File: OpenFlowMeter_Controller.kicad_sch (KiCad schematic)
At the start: 8 parts, among them J3 Conn_01x06, J5 Conn_01x03, U2 STM32F103C8Tx

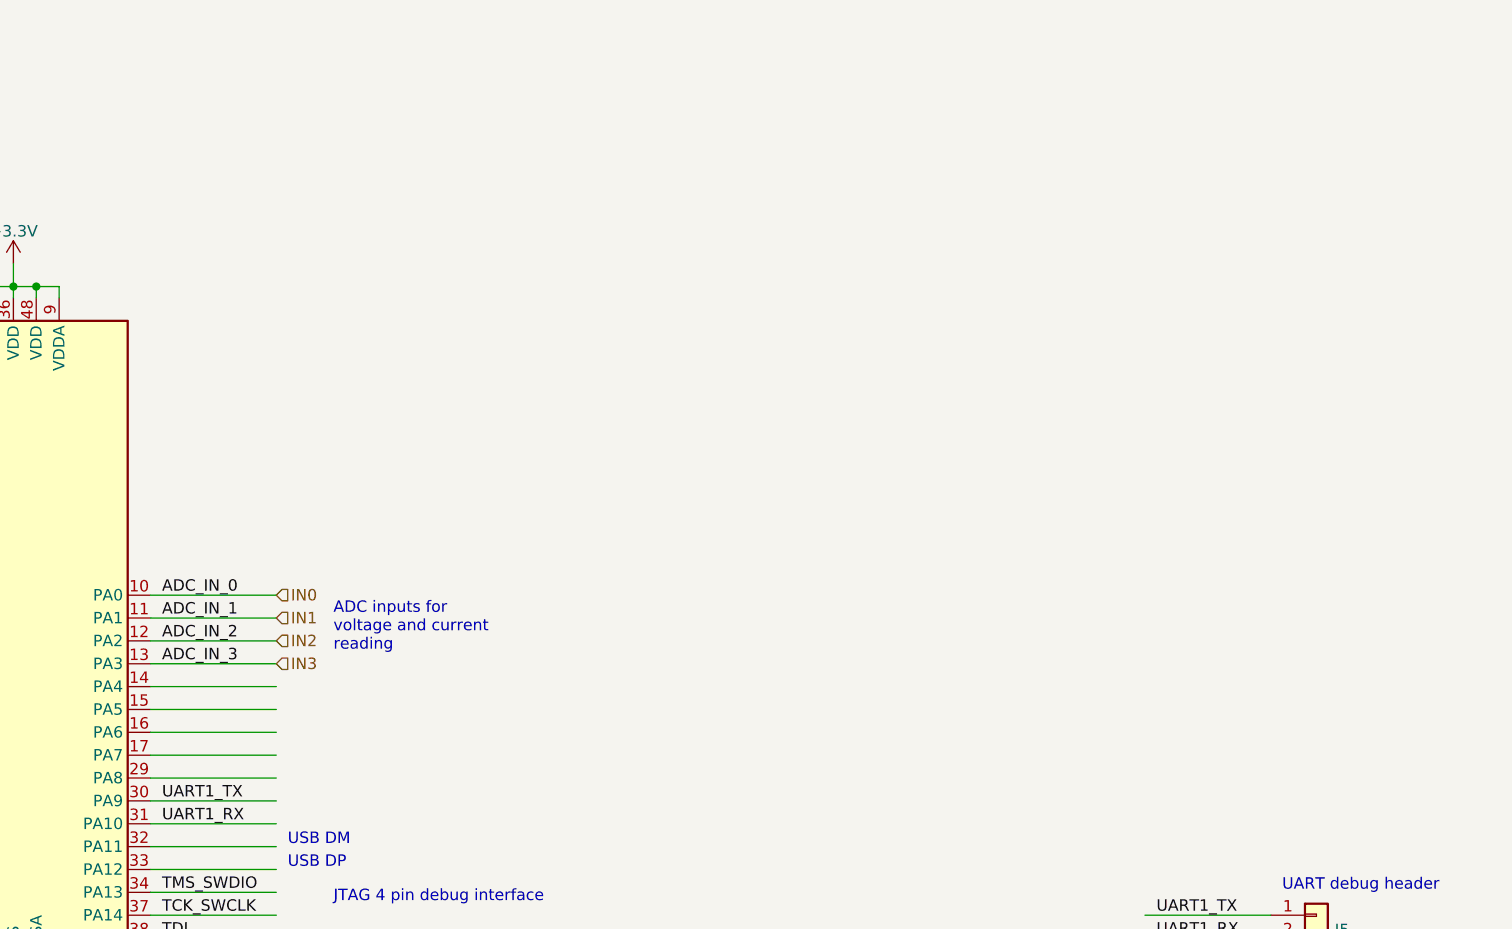
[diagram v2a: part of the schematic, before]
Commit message: added CAN Transceiver
added SN65HVD231 3.3V CAN Transceiver in order to connect multiple flow meter to a single bus.
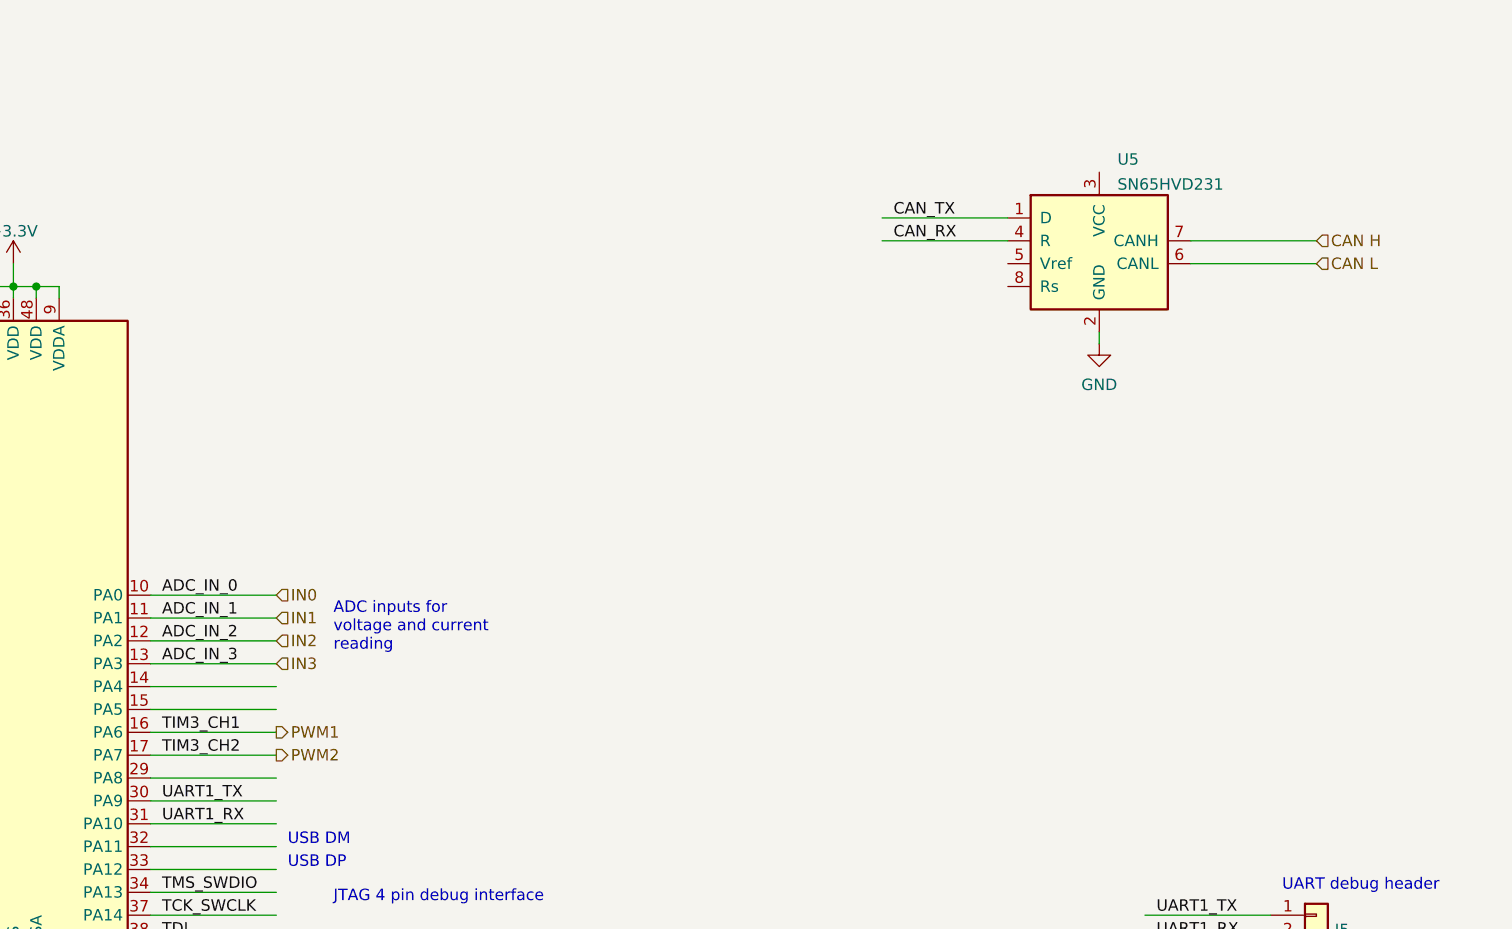
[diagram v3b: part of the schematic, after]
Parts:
- added U5: SN65HVD231, Package_SO:SOIC-8_3.9x4.9mm_P1.27mm, symbol Interface_CAN_LIN:SN65HVD231
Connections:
- net CAN_RX: now also U5.4 (R)
- net CAN_TX: now also U5.1 (D)
- net GND: now also U5.2 (GND)
- net PWM1: now reaches U2.16 (PA6)
- net PWM2: now reaches U2.17 (PA7)
- new net CAN H: U5.7 (CANH)
- new net CAN L: U5.6 (CANL)
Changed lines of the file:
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@@
+    (stroke (width 0) (type default) (color 0 0 0 0))
+  )
+  (wire (pts (xy 251.46 46.99) (xy 265.43 46.99))
     (stroke (width 0) (type default) (color 0 0 0 0))
   )
@@
     (stroke (width 0) (type default) (color 0 0 0 0))
   )
+  (wire (pts (xy 217.17 41.91) (xy 231.14 41.91))
+    (stroke (width 0) (type default) (color 0 0 0 0))
+  )
   (wire (pts (xy 260.35 124.46) (xy 259.08 124.46))
     (stroke (width 0) (type default) (color 0 0 0 0))
@@
     (stroke (width 0) (type default) (color 0 0 0 0))
   )
+  (wire (pts (xy 217.17 44.45) (xy 231.14 44.45))
+    (stroke (width 0) (type default) (color 0 0 0 0))
+  )
   (wire (pts (xy 88.9 111.76) (xy 102.87 111.76))
     (stroke (width 0) (type default) (color 0 0 0 0))
   )
+  (wire (pts (xy 241.3 54.61) (xy 241.3 55.88))
+    (stroke (width 0) (type default) (color 0 0 0 0))
+  )
   (wire (pts (xy 135.89 114.3) (xy 149.86 114.3))
     (stroke (width 0) (type default) (color 0 0 0 0))
@@
     (stroke (width 0) (type default) (color 0 0 0 0))
   )
+  (wire (pts (xy 251.46 44.45) (xy 265.43 44.45))
+    (stroke (width 0) (type default) (color 0 0 0 0))
+  )
   (wire (pts (xy 135.89 119.38) (xy 149.86 119.38))
     (stroke (width 0) (type default) (color 0 0 0 0))
@@
     (effects (font (size 1.27 1.27)) (justify left bottom))
   )
+  (label "TIM3_CH1" (at 137.16 99.06 0)
+    (effects (font (size 1.27 1.27)) (justify left bottom))
+  )
   (label "I2C2_SCL" (at 90.17 109.22 0)
     (effects (font (size 1.27 1.27)) (justify left bottom))
   )
+  (label "CAN_RX" (at 218.44 44.45 0)
+    (effects (font (size 1.27 1.27)) (justify left bottom))
+  )
   (label "UART1_RX" (at 247.65 121.92 0)
     (effects (font (size 1.27 1.27)) (justify left bottom))
@@
     (effects (font (size 1.27 1.27)) (justify left bottom))
   )
+  (label "CAN_TX" (at 218.44 41.91 0)
+    (effects (font (size 1.27 1.27)) (justify left bottom))
+  )
   (label "RCC_OSC_IN" (at 90.17 66.04 0)
     (effects (font (size 1.27 1.27)) (justify left bottom))
@@
   )
   (label "ADC_IN_3" (at 137.16 91.44 0)
+    (effects (font (size 1.27 1.27)) (justify left bottom))
+  )
+  (label "TIM3_CH2" (at 137.16 101.6 0)
     (effects (font (size 1.27 1.27)) (justify left bottom))
   )
@@
     (effects (font (size 1.27 1.27)) (justify left))
   )
+  (hierarchical_label "PWM1" (shape output) (at 149.86 99.06 0)
+    (effects (font (size 1.27 1.27)) (justify left))
+  )
   (hierarchical_label "IN0" (shape input) (at 149.86 83.82 0)
     (effects (font (size 1.27 1.27)) (justify left))
@@
     (effects (font (size 1.27 1.27)) (justify left))
   )
+  (hierarchical_label "CAN L" (shape input) (at 265.43 46.99 0)
+    (effects (font (size 1.27 1.27)) (justify left))
+  )
+  (hierarchical_label "CAN H" (shape input) (at 265.43 44.45 0)
+    (effects (font (size 1.27 1.27)) (justify left))
+  )
   (hierarchical_label "IN1" (shape input) (at 149.86 86.36 0)
+    (effects (font (size 1.27 1.27)) (justify left))
+  )
+  (hierarchical_label "PWM2" (shape output) (at 149.86 101.6 0)
     (effects (font (size 1.27 1.27)) (justify left))
   )
@@
     (pin "1")
   )
+  (symbol (lib_id "Interface_CAN_LIN:SN65HVD231") (at 241.3 44.45 0) (unit 1)
+    (in_bom yes) (on_board yes) (fields_autoplaced)
+    (property "Reference" "U5" (id 0) (at 243.3194 35.4035 0)
+      (effects (font (size 1.27 1.27)) (justify left))
+    )
+    (property "Value" "SN65HVD231" (id 1) (at 243.3194 38.1786 0)
+      (effects (font (size 1.27 1.27)) (justify left))
+    )
+    (property "Footprint" "Package_SO:SOIC-8_3.9x4.9mm_P1.27mm" (id 2) (at 241.3 57.15 0)
+      (effects (font (size 1.27 1.27)) hide)
+    )
+    (property "Datasheet" "http://www.ti.com/lit/ds/symlink/sn65hvd230.pdf" (id 3) (at 238.76 34.29 0)
+      (effects (font (size 1.27 1.27)) hide)
+    )
+    (pin "1")
+    (pin "2")
+    (pin "3")
+    (pin "4")
+    (pin "5")
+    (pin "6")
+    (pin "7")
+    (pin "8")
+  )
   (symbol (lib_id "power:GND") (at 19.05 45.72 0) (unit 1)
     (in_bom yes) (on_board yes)
@@
       (effects (font (size 1.27 1.27)) hide)
     )
+    (pin "1")
+  )
+  (symbol (lib_id "power:GND") (at 241.3 55.88 0) (unit 1)
+    (in_bom yes) (on_board yes) (fields_autoplaced)
+    (property "Reference" "#PWR041" (id 0) (at 241.3 62.23 0)
+      (effects (font (size 1.27 1.27)) hide)
+    )
+    (property "Value" "GND" (id 1) (at 241.3 60.4425 0))
+    (property "Footprint" "" (id 2) (at 241.3 55.88 0)
+      (effects (font (size 1.27 1.27)) hide)
+    )
+    (property "Datasheet" "" (id 3) (at 241.3 55.88 0)
+      (effects (font (size 1.27 1.27)) hide)
+    )

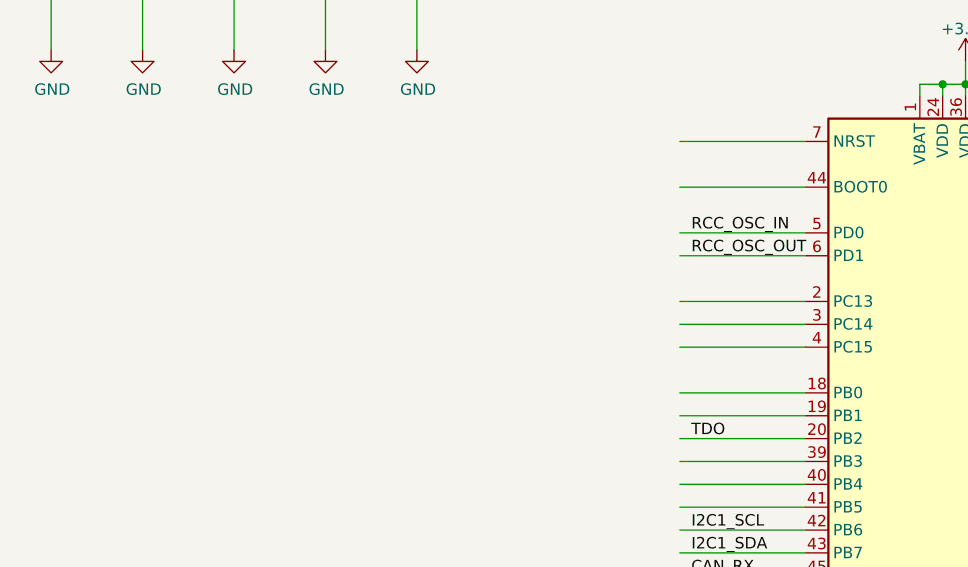
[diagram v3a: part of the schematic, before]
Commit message: Added crystal for STM32
added 12 MHz MT crystal for STM32's clock input
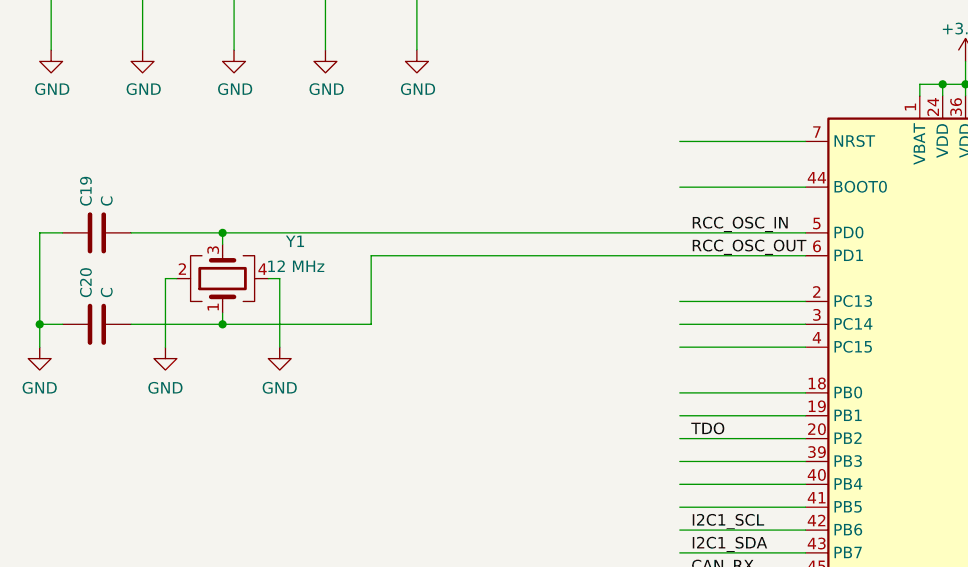
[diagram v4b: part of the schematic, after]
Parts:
- added C19, C20: C, Capacitor_SMD:C_0603_1608Metric_Pad1.08x0.95mm_HandSolder, symbol Device:C
- added Y1: 12 MHz, Crystal:Crystal_SMD_EuroQuartz_MT-4Pin_3.2x2.5mm_HandSoldering, symbol Device:Crystal_GND24
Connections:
- net GND: now also C19.1, C20.1, Y1.2, Y1.4
- net RCC_OSC_IN: now also C19.2, Y1.3
- net RCC_OSC_OUT: now also C20.2, Y1.1
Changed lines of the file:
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@@
     (rev "1")
   )
+  (junction (at 38.1 76.2) (diameter 0) (color 0 0 0 0)
+  )
   (junction (at 119.38 128.27) (diameter 0) (color 0 0 0 0)
   )
@@
   (junction (at 118.11 49.53) (diameter 0) (color 0 0 0 0)
   )
+  (junction (at 17.78 76.2) (diameter 0) (color 0 0 0 0)
+  )
   (junction (at 123.19 49.53) (diameter 0) (color 0 0 0 0)
   )
+  (junction (at 38.1 66.04) (diameter 0) (color 0 0 0 0)
+  )
   (junction (at 120.65 128.27) (diameter 0) (color 0 0 0 0)
   )
@@
     (stroke (width 0) (type default) (color 0 0 0 0))
   )
+  (wire (pts (xy 43.18 71.12) (xy 44.45 71.12))
+    (stroke (width 0) (type default) (color 0 0 0 0))
+  )
   (wire (pts (xy 39.37 39.37) (xy 39.37 45.72))
     (stroke (width 0) (type default) (color 0 0 0 0))
@@
     (stroke (width 0) (type default) (color 0 0 0 0))
   )
+  (wire (pts (xy 38.1 66.04) (xy 38.1 67.31))
+    (stroke (width 0) (type default) (color 0 0 0 0))
+  )
   (wire (pts (xy 88.9 76.2) (xy 102.87 76.2))
     (stroke (width 0) (type default) (color 0 0 0 0))
@@
     (stroke (width 0) (type default) (color 0 0 0 0))
   )
+  (wire (pts (xy 27.94 76.2) (xy 38.1 76.2))
+    (stroke (width 0) (type default) (color 0 0 0 0))
+  )
   (wire (pts (xy 119.38 128.27) (xy 119.38 129.54))
     (stroke (width 0) (type default) (color 0 0 0 0))
@@
     (stroke (width 0) (type default) (color 0 0 0 0))
   )
+  (wire (pts (xy 44.45 71.12) (xy 44.45 78.74))
+    (stroke (width 0) (type default) (color 0 0 0 0))
+  )
   (wire (pts (xy 135.89 83.82) (xy 149.86 83.82))
     (stroke (width 0) (type default) (color 0 0 0 0))
@@
     (stroke (width 0) (type default) (color 0 0 0 0))
   )
+  (wire (pts (xy 17.78 66.04) (xy 17.78 76.2))
+    (stroke (width 0) (type default) (color 0 0 0 0))
+  )
   (wire (pts (xy 115.57 128.27) (xy 118.11 128.27))
     (stroke (width 0) (type default) (color 0 0 0 0))
@@
     (stroke (width 0) (type default) (color 0 0 0 0))
   )
+  (wire (pts (xy 20.32 66.04) (xy 17.78 66.04))
+    (stroke (width 0) (type default) (color 0 0 0 0))
+  )
   (wire (pts (xy 259.08 138.43) (xy 259.08 140.97))
     (stroke (width 0) (type default) (color 0 0 0 0))
@@
     (stroke (width 0) (type default) (color 0 0 0 0))
   )
+  (wire (pts (xy 38.1 76.2) (xy 54.61 76.2))
+    (stroke (width 0) (type default) (color 0 0 0 0))
+  )
   (wire (pts (xy 135.89 111.76) (xy 149.86 111.76))
     (stroke (width 0) (type default) (color 0 0 0 0))
@@
     (stroke (width 0) (type default) (color 0 0 0 0))
   )
+  (wire (pts (xy 33.02 71.12) (xy 31.75 71.12))
+    (stroke (width 0) (type default) (color 0 0 0 0))
+  )
   (wire (pts (xy 88.9 55.88) (xy 102.87 55.88))
     (stroke (width 0) (type default) (color 0 0 0 0))
@@
     (stroke (width 0) (type default) (color 0 0 0 0))
   )
+  (wire (pts (xy 54.61 76.2) (xy 54.61 68.58))
+    (stroke (width 0) (type default) (color 0 0 0 0))
+  )
   (wire (pts (xy 135.89 91.44) (xy 149.86 91.44))
     (stroke (width 0) (type default) (color 0 0 0 0))
@@
     (stroke (width 0) (type default) (color 0 0 0 0))
   )
-  (wire (pts (xy 88.9 68.58) (xy 102.87 68.58))
+  (wire (pts (xy 54.61 68.58) (xy 102.87 68.58))
     (stroke (width 0) (type default) (color 0 0 0 0))
   )
@@
     (stroke (width 0) (type default) (color 0 0 0 0))
   )
+  (wire (pts (xy 27.94 66.04) (xy 38.1 66.04))
+    (stroke (width 0) (type default) (color 0 0 0 0))
+  )
   (wire (pts (xy 135.89 109.22) (xy 149.86 109.22))
     (stroke (width 0) (type default) (color 0 0 0 0))
@@
     (stroke (width 0) (type default) (color 0 0 0 0))
   )
+  (wire (pts (xy 17.78 76.2) (xy 17.78 78.74))
+    (stroke (width 0) (type default) (color 0 0 0 0))
+  )
   (wire (pts (xy 123.19 49.53) (xy 123.19 50.8))
     (stroke (width 0) (type default) (color 0 0 0 0))
@@
     (stroke (width 0) (type default) (color 0 0 0 0))
   )
-  (wire (pts (xy 88.9 66.04) (xy 102.87 66.04))
+  (wire (pts (xy 38.1 66.04) (xy 102.87 66.04))
     (stroke (width 0) (type default) (color 0 0 0 0))
   )
@@
     (stroke (width 0) (type default) (color 0 0 0 0))
   )
+  (wire (pts (xy 17.78 76.2) (xy 20.32 76.2))
+    (stroke (width 0) (type default) (color 0 0 0 0))
+  )
+  (wire (pts (xy 31.75 71.12) (xy 31.75 78.74))
+    (stroke (width 0) (type default) (color 0 0 0 0))
+  )
   (wire (pts (xy 19.05 39.37) (xy 19.05 45.72))
     (stroke (width 0) (type default) (color 0 0 0 0))
   )
   (wire (pts (xy 259.08 148.59) (xy 259.08 157.48))
+    (stroke (width 0) (type default) (color 0 0 0 0))
+  )
+  (wire (pts (xy 38.1 74.93) (xy 38.1 76.2))
     (stroke (width 0) (type default) (color 0 0 0 0))
   )
@@
     (pin "3")
   )
+  (symbol (lib_id "power:GND") (at 17.78 78.74 0) (unit 1)
+    (in_bom yes) (on_board yes) (fields_autoplaced)
+    (property "Reference" "#PWR044" (id 0) (at 17.78 85.09 0)
+      (effects (font (size 1.27 1.27)) hide)
+    )
+    (property "Value" "GND" (id 1) (at 17.78 83.3025 0))
+    (property "Footprint" "" (id 2) (at 17.78 78.74 0)
+      (effects (font (size 1.27 1.27)) hide)
+    )
+    (property "Datasheet" "" (id 3) (at 17.78 78.74 0)
+      (effects (font (size 1.27 1.27)) hide)
+    )
+    (pin "1")
+  )
   (symbol (lib_id "Device:C") (at 39.37 35.56 0) (unit 1)
     (in_bom yes) (on_board yes)
@@
     (pin "1")
   )
+  (symbol (lib_id "power:GND") (at 44.45 78.74 0) (unit 1)
+    (in_bom yes) (on_board yes) (fields_autoplaced)
+    (property "Reference" "#PWR043" (id 0) (at 44.45 85.09 0)
+      (effects (font (size 1.27 1.27)) hide)
+    )
+    (property "Value" "GND" (id 1) (at 44.45 83.3025 0))
+    (property "Footprint" "" (id 2) (at 44.45 78.74 0)
+      (effects (font (size 1.27 1.27)) hide)
+    )
+    (property "Datasheet" "" (id 3) (at 44.45 78.74 0)
+      (effects (font (size 1.27 1.27)) hide)
+    )
+    (pin "1")
+  )
   (symbol (lib_id "power:+3.3V") (at 29.21 25.4 0) (unit 1)
     (in_bom yes) (on_board yes)
@@
     )
     (pin "1")
+  )
+  (symbol (lib_id "Device:Crystal_GND24") (at 38.1 71.12 90) (unit 1)
+    (in_bom yes) (on_board yes) (fields_autoplaced)
+    (property "Reference" "Y1" (id 0) (at 46.2227 67.0265 90))
+    (property "Value" "12 MHz" (id 1) (at 46.2227 69.8016 90))
+    (property "Footprint" "Crystal:Crystal_SMD_EuroQuartz_MT-4Pin_3.2x2.5mm_HandSoldering" (id 2) (at 38.1 71.12 0)
+      (effects (font (size 1.27 1.27)) hide)
+    )
+    (property "Datasheet" "~" (id 3) (at 38.1 71.12 0)
+      (effects (font (size 1.27 1.27)) hide)
+    )
+    (pin "1")
+    (pin "2")
+    (pin "3")
+    (pin "4")
   )
   (symbol (lib_id "Interface_CAN_LIN:SN65HVD231") (at 241.3 44.45 0) (unit 1)
@@
     (pin "1")
   )
+  (symbol (lib_id "Device:C") (at 24.13 66.04 90) (unit 1)
+    (in_bom yes) (on_board yes)
+    (property "Reference" "C19" (id 0) (at 22.9616 63.119 0)
+      (effects (font (size 1.27 1.27)) (justify left))
+    )
+    (property "Value" "C" (id 1) (at 25.273 63.119 0)
+      (effects (font (size 1.27 1.27)) (justify left))
+    )
+    (property "Footprint" "Capacitor_SMD:C_0603_1608Metric_Pad1.08x0.95mm_HandSolder" (id 2) (at 27.94 65.0748 0)
+      (effects (font (size 1.27 1.27)) hide)
+    )
+    (property "Datasheet" "~" (id 3) (at 24.13 66.04 0)
+      (effects (font (size 1.27 1.27)) hide)
+    )
+    (pin "1")
+    (pin "2")
+  )
   (symbol (lib_id "Device:C") (at 59.69 35.56 0) (unit 1)
     (in_bom yes) (on_board yes)
@@
       (effects (font (size 1.27 1.27)) hide)
     )
+    (pin "1")
+  )
+  (symbol (lib_id "Device:C") (at 24.13 76.2 90) (unit 1)
+    (in_bom yes) (on_board yes)
+    (property "Reference" "C20" (id 0) (at 22.9616 73.279 0)
+      (effects (font (size 1.27 1.27)) (justify left))
+    )
+    (property "Value" "C" (id 1) (at 25.273 73.279 0)
+      (effects (font (size 1.27 1.27)) (justify left))
+    )
+    (property "Footprint" "Capacitor_SMD:C_0603_1608Metric_Pad1.08x0.95mm_HandSolder" (id 2) (at 27.94 75.2348 0)
+      (effects (font (size 1.27 1.27)) hide)
+    )
+    (property "Datasheet" "~" (id 3) (at 24.13 76.2 0)
+      (effects (font (size 1.27 1.27)) hide)
+    )
+    (pin "1")
+    (pin "2")
+  )
+  (symbol (lib_id "power:GND") (at 31.75 78.74 0) (unit 1)
+    (in_bom yes) (on_board yes) (fields_autoplaced)
+    (property "Reference" "#PWR042" (id 0) (at 31.75 85.09 0)
+      (effects (font (size 1.27 1.27)) hide)
+    )
+    (property "Value" "GND" (id 1) (at 31.75 83.3025 0))
+    (property "Footprint" "" (id 2) (at 31.75 78.74 0)
+      (effects (font (size 1.27 1.27)) hide)
+    )
+    (property "Datasheet" "" (id 3) (at 31.75 78.74 0)
+      (effects (font (size 1.27 1.27)) hide)
+    )
